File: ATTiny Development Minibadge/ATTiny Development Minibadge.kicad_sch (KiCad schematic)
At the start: 16 parts, among them J1 SPI, J2 I2C, J3 DAC, J4 USART, U1 ATtiny816-M

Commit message: Board revision R5
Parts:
- J1, J4: footprint Connector_PinHeader_2.54mm:PinHeader_1x04_P2.54mm_Vertical -> Connector_PinHeader_2.54mm:PinHeader_1x05_P2.54mm_Vertical; symbol Connector_Generic:Conn_01x04 -> Connector_Generic:Conn_01x05
- U1: value ATtiny816-M -> ATtiny816/1616-M
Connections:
- net GND: now also J1.1 (Pin_1), J4.1 (Pin_1)
- net SPI_MISO: now also J1.4 (Pin_4); no longer J1.3 (Pin_3)
- net SPI_MOSI: now also J1.5 (Pin_5); no longer J1.4 (Pin_4)
- net SPI_SCK: now also J1.3 (Pin_3); no longer J1.2 (Pin_2)
- net SPI_SS: now also J1.2 (Pin_2); no longer J1.1 (Pin_1)
- net USART_RXD: now also J4.4 (Pin_4); no longer J4.3 (Pin_3)
- net USART_TXD: now also J4.5 (Pin_5); no longer J4.4 (Pin_4)
- net USART_XCK: now also J4.3 (Pin_3); no longer J4.2 (Pin_2)
- net USART_XDIR: now also J4.2 (Pin_2); no longer J4.1 (Pin_1)
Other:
- note added: "ATTiny816/1616"
- note removed: "ATTiny816"
- title: (none) -> ATTiny Minibadge Devboard
- moved on the sheet: C1, D1, D2, J2, J3, MB1, R1, R2, R3, TP1, TP2, TP3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

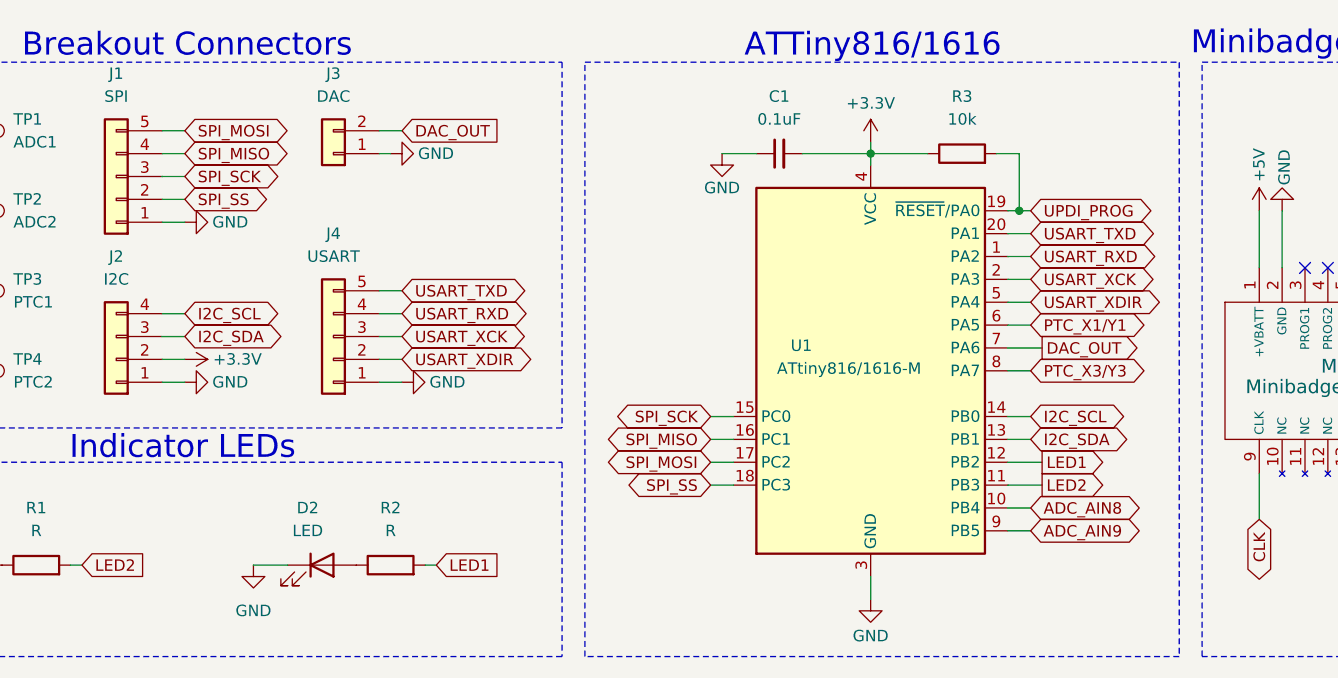
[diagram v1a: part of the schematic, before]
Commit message: R6
Add diode for reverse polarity protection
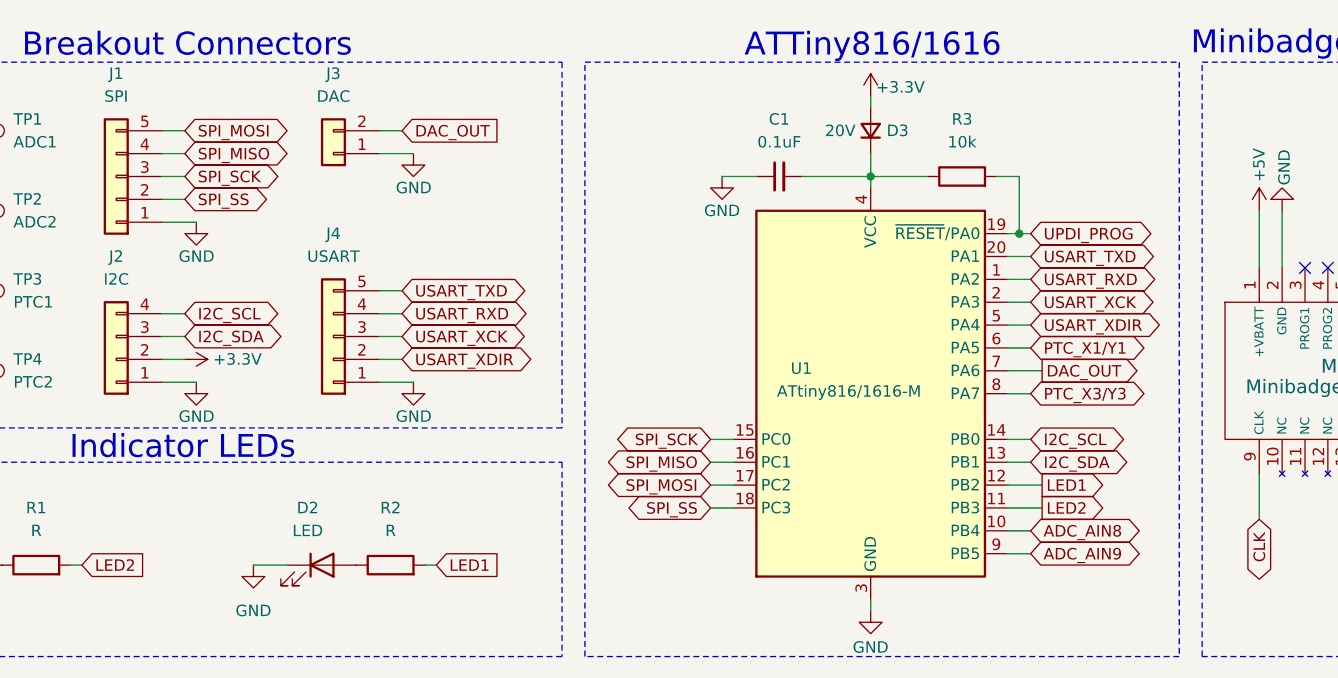
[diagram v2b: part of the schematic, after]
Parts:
- added D3: 20V, Diode_SMD:D_0603_1608Metric, symbol Device:D_Small
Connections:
- net +3.3V: now also D3.2 (A); no longer C1.2, R3.1, U1.4 (VCC)
- new net: C1.2, D3.1 (K), R3.1, U1.4 (VCC)
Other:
- moved on the sheet: C1, R3, U1
